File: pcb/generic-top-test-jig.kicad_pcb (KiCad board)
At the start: 2 copper layers, 45 x 39.2 mm, 13 parts, among them P1 CONN_01X16, U1 74HC4051, U2 74HC4067, U3 74HC4067, U4 74HC4067, U5 74HC4067

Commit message: Gerbers for v1 of the test jig.
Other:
- net class Default: clearance 0.1524 -> 0.14986
- net class Power: clearance 0.1524 -> 0.14986
- rule trace_clearance: 0.1524 -> 0.14986

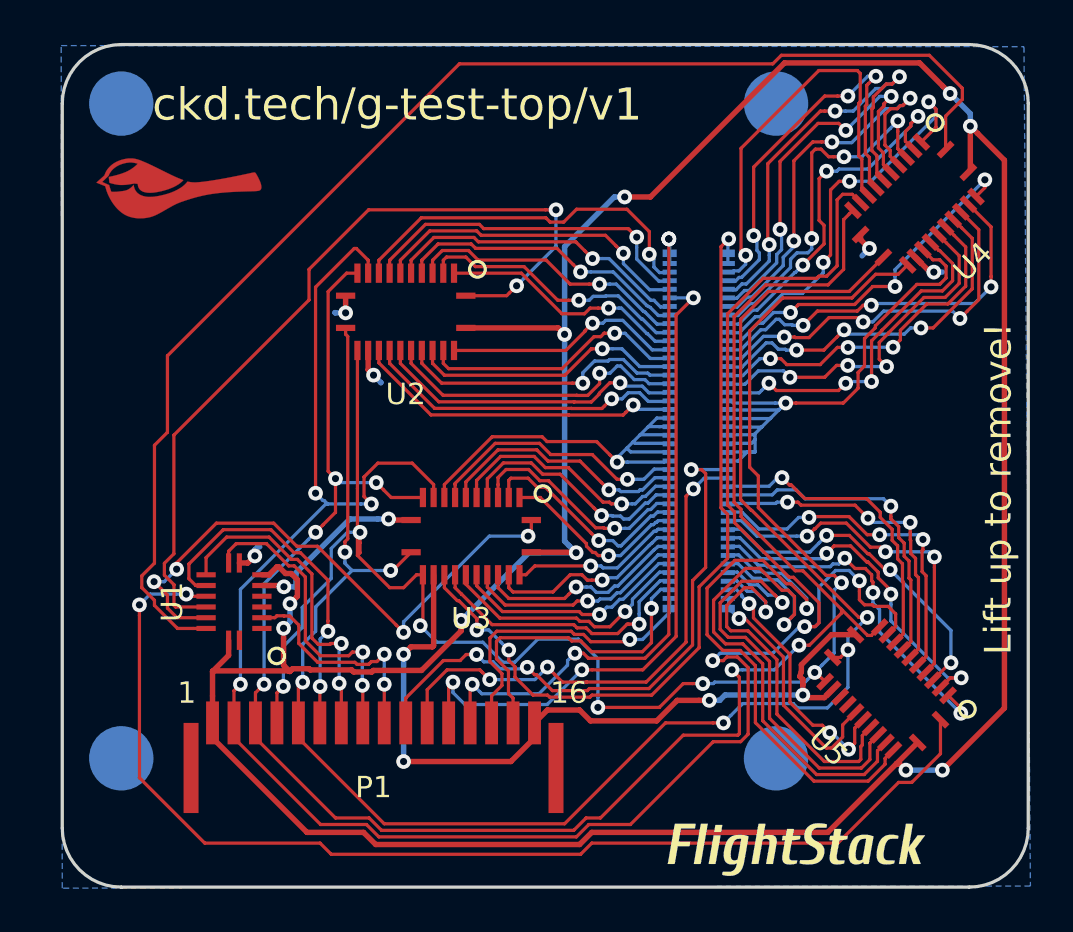
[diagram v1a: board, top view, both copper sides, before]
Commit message: Generic Test Jig Top v2 which correct Vee input in 8-way mux and changes SWD pins.
Also:
* Switches to thinner FlightStack logo.
* Adds OSHW logo.
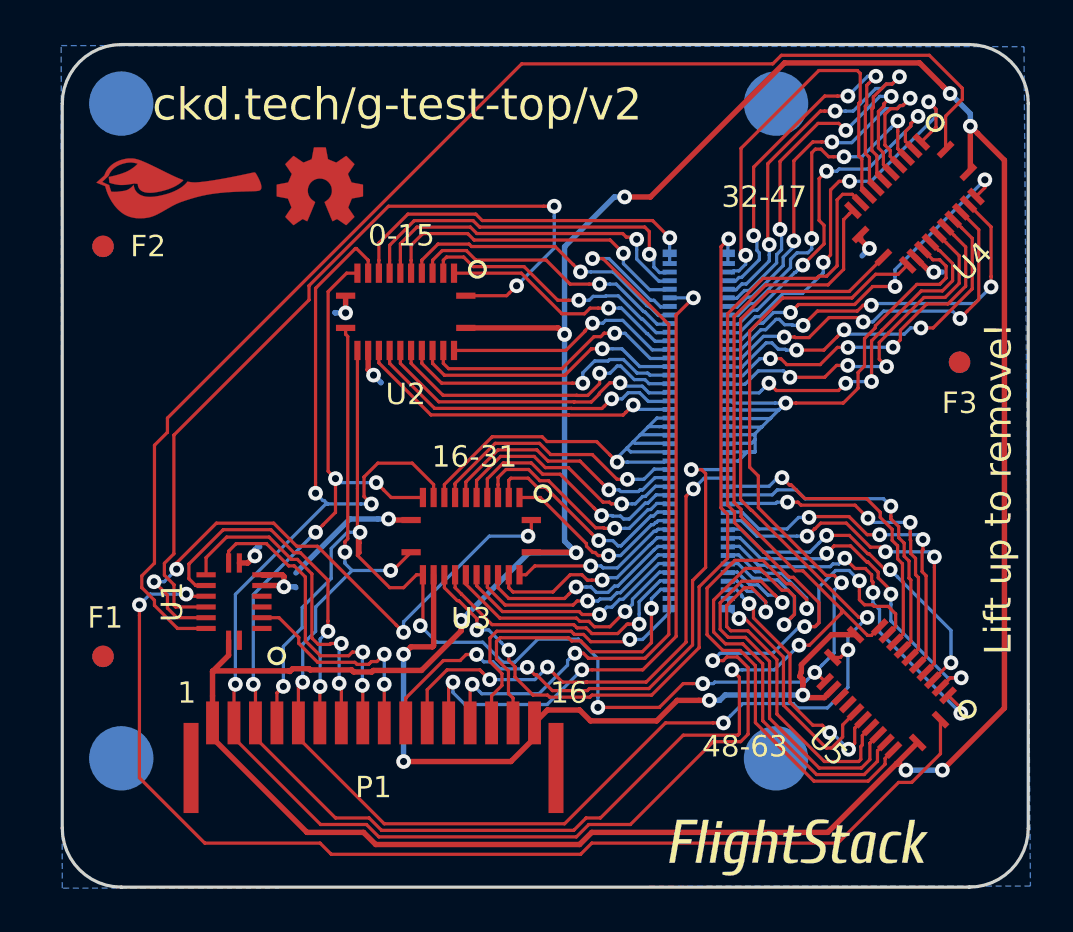
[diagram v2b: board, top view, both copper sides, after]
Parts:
- removed the G*** at (164.2, 127.5)
- added F1: 1mm, macrofab:Fiducial, F.Cu at (131.9, 118.5)
- added F2: 1mm, macrofab:Fiducial, F.Cu at (131.9, 99.4)
- added F3: 1mm, macrofab:Fiducial, F.Cu at (171.8, 104.8)
- added F4: 1mm, macrofab:Fiducial, B.Cu at (131.9, 118.5)
- added F5: 1mm, macrofab:Fiducial, B.Cu at (131.9, 99.4)
- added F6: 1mm, macrofab:Fiducial, B.Cu at (171.8, 104.8)
- added G***: LOGO, flightstack:flightstack_thin-12mm, F.Cu at (164.3, 127.4)
- added G***: OSHW, oshw:oshw-4mm, F.Cu at (142.0, 96.6)
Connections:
- PORT_IN1 pad 1: /SWCLK -> /TIM1
- PORT_IN1 pad 6: /GPIO2 -> /SWCLK
- U1 pad 7: +5V -> GNDPWR
- U2 pad 6: /GPIO2 -> /TIM4
- U2 pad 7: /TIM4 -> /TIM3
- U2 pad 8: /TIM3 -> /TIM2
- U2 pad 9: /TIM2 -> /TIM1
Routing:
- net /TIM1: track 0.00 -> 17.2 mm, vias 0 -> 1
- net /GPIO2: track 14.2 -> 0.00 mm, vias 1 -> 0
- net +5V: track 149.7 -> 143.0 mm, vias 10 -> 8
- net /SWCLK: track 32.2 -> 36.3 mm, vias 4 -> 3
- net /Z2: track 61.9 -> 60.2 mm
- net GNDPWR: track 52.8 -> 54.0 mm
- net /TIM2: track 17.2 -> 16.5 mm
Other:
- board text added: "0-15"
- board text added: "16-31"
- board text added: "32-47"
- board text added: "48-63"
- board text added: "ckd.tech/g-test-top/v2"
- board text removed: "ckd.tech/g-test-top/v1"

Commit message: Add decoupling caps.
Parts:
- added C1: 0.1uF, Capacitors_SMD:C_0603_HandSoldering, B.Cu at (149.1, 112.9)
- added C2: 0.1uF, Capacitors_SMD:C_0603_HandSoldering, B.Cu at (138.0, 116.0)
- added C3: 0.1uF, Capacitors_SMD:C_0603_HandSoldering, B.Cu at (145.9, 102.5)
- added C4: 0.1uF, Capacitors_SMD:C_0603_HandSoldering, B.Cu at (169.7, 97.4)
- added C5: 0.1uF, Capacitors_SMD:C_0603_HandSoldering, B.Cu at (168.4, 120.0)
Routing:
- net +5V: track 143.0 -> 156.6 mm, vias 8 -> 11
- net GNDPWR: track 54.0 -> 59.8 mm
- net /Z1: track 27.3 -> 28.8 mm
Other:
- board text added: "ckd.tech/g-test-top/v3"
- board text removed: "ckd.tech/g-test-top/v2"

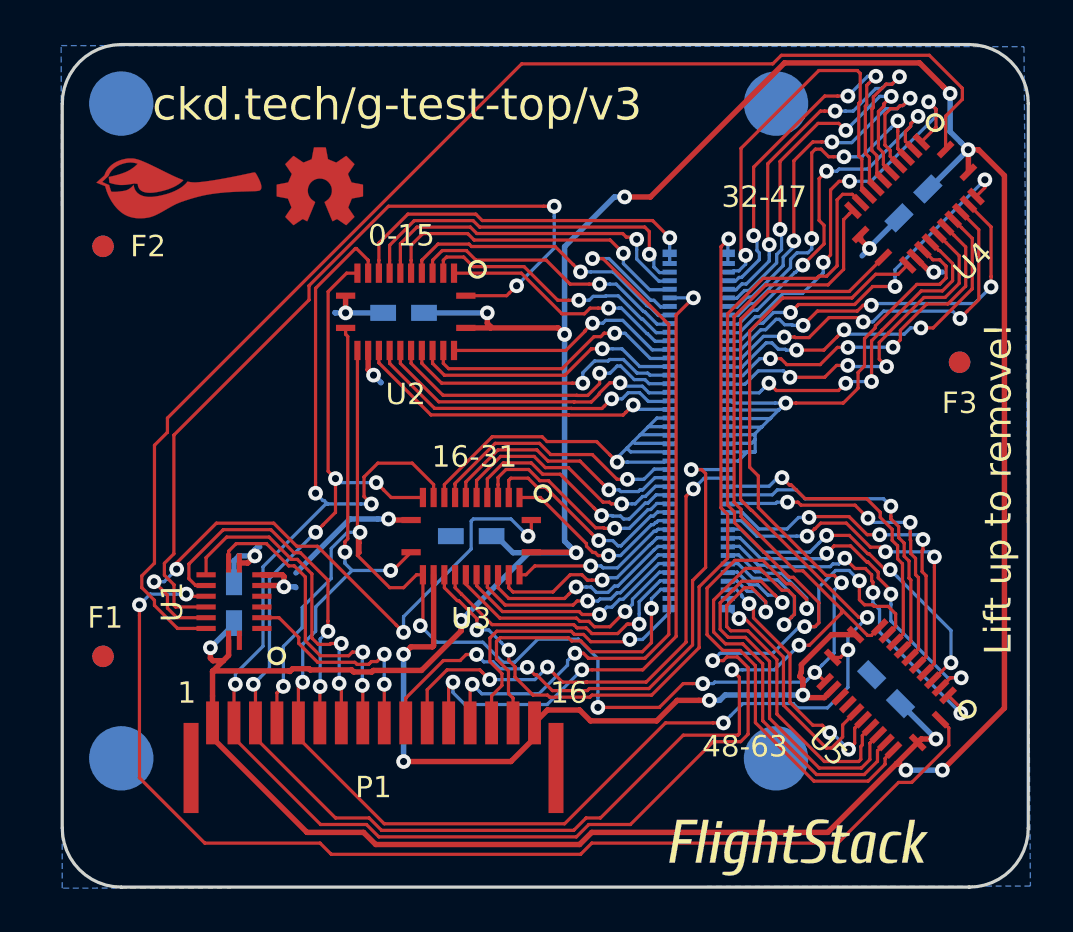
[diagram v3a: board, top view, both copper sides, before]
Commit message: Rebrand everything to Polystack and increment versions.
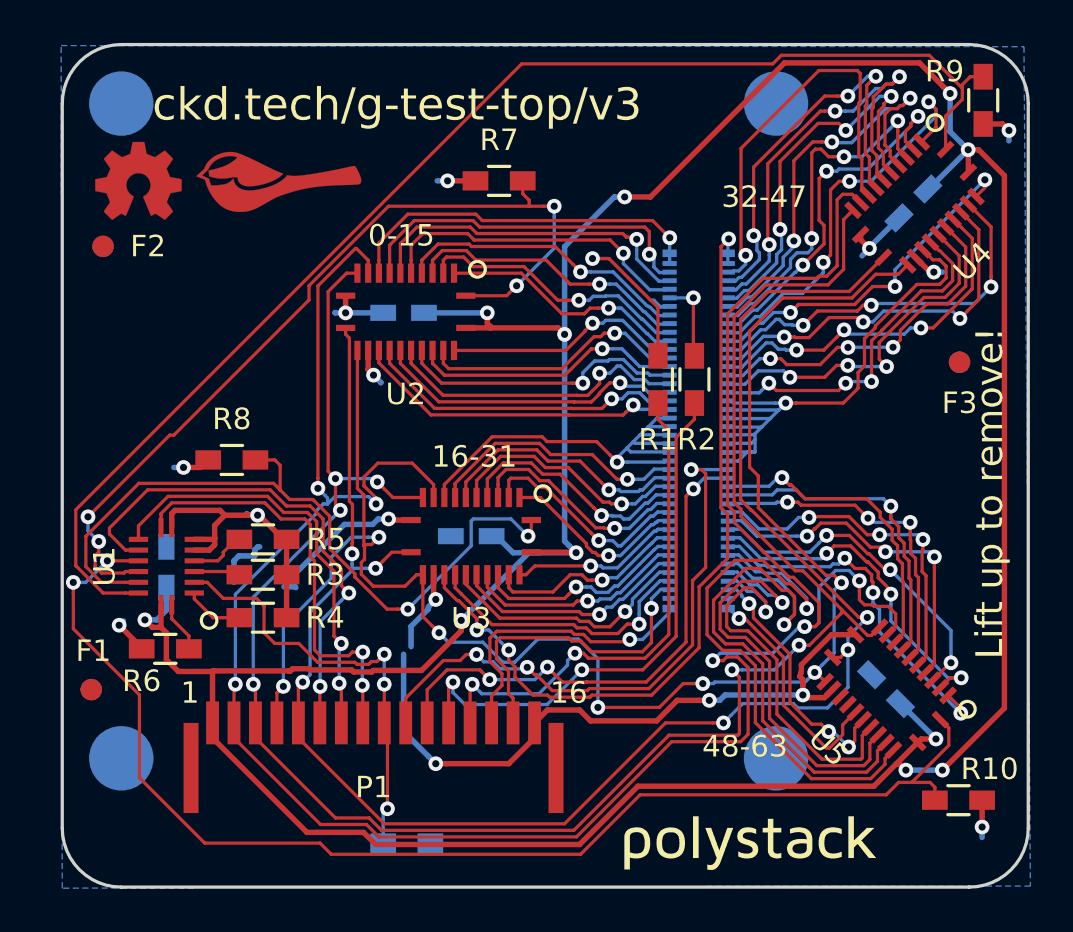
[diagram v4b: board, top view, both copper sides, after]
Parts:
- removed the G*** at (164.3, 127.4)
- added R1: 220, Resistors_SMD:R_0603_HandSoldering, F.Cu at (157.8, 105.6)
- added R10: 10k, Resistors_SMD:R_0603_HandSoldering, F.Cu at (171.8, 125.2)
- added R11: 10k, Resistors_SMD:R_0603_HandSoldering, B.Cu at (146.1, 127.2)
- added R2: 220, Resistors_SMD:R_0603_HandSoldering, F.Cu at (159.4, 105.6)
- added R3: 10k, Resistors_SMD:R_0603_HandSoldering, F.Cu at (139.3, 114.7)
- added R4: 10k, Resistors_SMD:R_0603_HandSoldering, F.Cu at (139.3, 116.7)
- added R5: 10k, Resistors_SMD:R_0603_HandSoldering, F.Cu at (139.3, 113.0)
- added R6: 10k, Resistors_SMD:R_0603_HandSoldering, F.Cu at (134.8, 118.2)
- added R7: 10k, Resistors_SMD:R_0603_HandSoldering, F.Cu at (150.3, 96.3)
- added R8: 10k, Resistors_SMD:R_0603_HandSoldering, F.Cu at (137.9, 109.3)
- added R9: 10k, Resistors_SMD:R_0603_HandSoldering, F.Cu at (172.9, 92.6)
- added svg2mod: G***, polystack:polystack-medium-0.625, B.Cu at (162.1, 127.2)
- added svg2mod: G***, polystack:polystack-medium-0.625, F.Cu at (162.1, 127.2)
- moved G*** 8.45 mm to (133.6, 96.3)
- moved G*** 4.66 mm to (140.1, 96.4)
- moved C2 3.56 mm to (134.8, 114.3)
- moved U1 3.56 mm to (134.8, 114.3)
- moved F1 1.64 mm to (131.3, 120.0)
- moved F4 1.64 mm to (131.3, 120.0)
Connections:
- P1 pad 12: /SWDIO -> Net-(P1-Pad12)
- P1 pad 13: /SWCLK -> Net-(P1-Pad13)
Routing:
- net /SWDIO: track 31.6 -> 3.83 mm, vias 3 -> 1
- net /SWCLK: track 36.3 -> 10.6 mm, vias 3 -> 1
- net Net-(P1-Pad12): track 0.00 -> 25.6 mm, vias 0 -> 2
- net Net-(P1-Pad13): track 0.00 -> 23.6 mm, vias 0 -> 2
- net GNDPWR: track 59.8 -> 74.4 mm, vias 11 -> 15
- net /Z: track 10.2 -> 20.3 mm, vias 2 -> 3
- net /S4: track 16.5 -> 23.8 mm
- net /Z1: track 28.8 -> 35.1 mm, vias 4 -> 2
- net /S6: track 14.2 -> 19.9 mm
- net /S5: track 15.1 -> 19.9 mm
- net /Z3: track 54.0 -> 58.2 mm
- net +5V: track 156.6 -> 160.2 mm
- net (no net): track 0.00 -> 3.21 mm
- net Net-(R4-Pad2): track 0.00 -> 2.74 mm
- net Net-(R5-Pad2): track 0.00 -> 2.60 mm
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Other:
- rule pad_to_mask_clearance: 0.2 -> 0.0762

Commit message: Final gerbers for test manufacturing run.
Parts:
- moved P1 0.90 mm to (144.5, 123.2)
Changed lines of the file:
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@@
 (kicad_pcb (version 4) (host pcbnew 4.0.1-stable)
   (general
-    (links 0)
+    (links 154)
     (no_connects 0)
-    (area 129.924999 89.924999 175.075001 129.325001)
+    (area 118.127143 74.1 268.690476 178)
     (thickness 1.6)
     (drawings 33)
@@
     (visible_elements FFFFFF7F)
     (pcbplotparams
-      (layerselection 0x010f0_80000001)
+      (layerselection 0x010fc_80000001)
       (usegerberextensions true)
       (excludeedgelayer true)
@@
     (add_net +5V)
     (add_net GNDPWR)
+  )
+  (module fci:SFW12LF-16pin (layer F.Cu)
+    (at 144.5 123.2)
+    (fp_text reference P1 (at 0 1.4) (layer F.SilkS)
+      (effects (font (size 1 1) (thickness 0.15)))
+    )
+    (fp_text value CONN_01X16 (at 0 0.4) (layer F.Fab)
+      (effects (font (size 1 1) (thickness 0.15)))
+    )
+    (fp_line (start -11 6) (end 11 6) (layer F.CrtYd) (width 0.15))
+    (pad 1 smd rect (at -7.5 -1.6) (size 0.6 2) (layers F.Cu F.Paste F.Mask)
+      (net 2 +5V))
+    (pad 2 smd rect (at -6.5 -1.6) (size 0.6 2) (layers F.Cu F.Paste F.Mask)
+      (net 3 /S0))
+    (pad 3 smd rect (at -5.5 -1.6) (size 0.6 2) (layers F.Cu F.Paste F.Mask)
+      (net 4 /S1))
+    (pad 4 smd rect (at -4.5 -1.6) (size 0.6 2) (layers F.Cu F.Paste F.Mask)
+      (net 5 /S2))
+    (pad 5 smd rect (at -3.5 -1.6) (size 0.6 2) (layers F.Cu F.Paste F.Mask)
+      (net 6 /S3))
+    (pad 6 smd rect (at -2.5 -1.6) (size 0.6 2) (layers F.Cu F.Paste F.Mask)
+      (net 7 /S4))
+    (pad 7 smd rect (at -1.5 -1.6) (size 0.6 2) (layers F.Cu F.Paste F.Mask)
+      (net 8 /S5))
+    (pad 8 smd rect (at -0.5 -1.6) (size 0.6 2) (layers F.Cu F.Paste F.Mask)
+      (net 9 /S6))
+    (pad 9 smd rect (at 0.5 -1.6) (size 0.6 2) (layers F.Cu F.Paste F.Mask)
+      (net 10 /Z))
+    (pad 10 smd rect (at 1.5 -1.6) (size 0.6 2) (layers F.Cu F.Paste F.Mask)
+      (net 11 /BOOT))
+    (pad 11 smd rect (at 2.5 -1.6) (size 0.6 2) (layers F.Cu F.Paste F.Mask)
+      (net 12 /RESET))
+    (pad 12 smd rect (at 3.5 -1.6) (size 0.6 2) (layers F.Cu F.Paste F.Mask)
+      (net 85 "Net-(P1-Pad12)"))
+    (pad 13 smd rect (at 4.5 -1.6) (size 0.6 2) (layers F.Cu F.Paste F.Mask)
+      (net 86 "Net-(P1-Pad13)"))
+    (pad 14 smd rect (at 5.5 -1.6) (size 0.6 2) (layers F.Cu F.Paste F.Mask)
+      (net 15 /RX))
+    (pad 15 smd rect (at 6.5 -1.6) (size 0.6 2) (layers F.Cu F.Paste F.Mask)
+      (net 16 /TX))
+    (pad 16 smd rect (at 7.5 -1.6) (size 0.6 2) (layers F.Cu F.Paste F.Mask)
+      (net 1 GNDPWR))
+    (pad "" smd rect (at -8.5 0.5) (size 0.7 4.2) (layers F.Cu F.Paste F.Mask))
+    (pad "" smd rect (at 8.5 0.5) (size 0.7 4.2) (layers F.Cu F.Paste F.Mask))
   )
   (module polystack:polystack-medium-0.625 (layer B.Cu)
@@
       (net 16 /TX))
   )
-  (module fci:SFW12LF-16pin (layer F.Cu)
-    (at 144.5 124.1)
-    (fp_text reference P1 (at 0 0.5) (layer F.SilkS)
-      (effects (font (size 1 1) (thickness 0.15)))
-    )
-    (fp_text value CONN_01X16 (at 0 -0.5) (layer F.Fab)
-      (effects (font (size 1 1) (thickness 0.15)))
-    )
-    (fp_line (start -11 5.1) (end 11 5.1) (layer F.CrtYd) (width 0.15))
-    (pad 1 smd rect (at -7.5 -2.5) (size 0.6 2) (layers F.Cu F.Paste F.Mask)
-      (net 2 +5V))
-    (pad 2 smd rect (at -6.5 -2.5) (size 0.6 2) (layers F.Cu F.Paste F.Mask)
-      (net 3 /S0))
-    (pad 3 smd rect (at -5.5 -2.5) (size 0.6 2) (layers F.Cu F.Paste F.Mask)
-      (net 4 /S1))
-    (pad 4 smd rect (at -4.5 -2.5) (size 0.6 2) (layers F.Cu F.Paste F.Mask)
-      (net 5 /S2))
-    (pad 5 smd rect (at -3.5 -2.5) (size 0.6 2) (layers F.Cu F.Paste F.Mask)
-      (net 6 /S3))
-    (pad 6 smd rect (at -2.5 -2.5) (size 0.6 2) (layers F.Cu F.Paste F.Mask)
-      (net 7 /S4))
-    (pad 7 smd rect (at -1.5 -2.5) (size 0.6 2) (layers F.Cu F.Paste F.Mask)
-      (net 8 /S5))
-    (pad 8 smd rect (at -0.5 -2.5) (size 0.6 2) (layers F.Cu F.Paste F.Mask)
-      (net 9 /S6))
-    (pad 9 smd rect (at 0.5 -2.5) (size 0.6 2) (layers F.Cu F.Paste F.Mask)
-      (net 10 /Z))
-    (pad 10 smd rect (at 1.5 -2.5) (size 0.6 2) (layers F.Cu F.Paste F.Mask)
-      (net 11 /BOOT))
-    (pad 11 smd rect (at 2.5 -2.5) (size 0.6 2) (layers F.Cu F.Paste F.Mask)
-      (net 12 /RESET))
-    (pad 12 smd rect (at 3.5 -2.5) (size 0.6 2) (layers F.Cu F.Paste F.Mask)
-      (net 85 "Net-(P1-Pad12)"))
-    (pad 13 smd rect (at 4.5 -2.5) (size 0.6 2) (layers F.Cu F.Paste F.Mask)
-      (net 86 "Net-(P1-Pad13)"))
-    (pad 14 smd rect (at 5.5 -2.5) (size 0.6 2) (layers F.Cu F.Paste F.Mask)
-      (net 15 /RX))
-    (pad 15 smd rect (at 6.5 -2.5) (size 0.6 2) (layers F.Cu F.Paste F.Mask)
-      (net 16 /TX))
-    (pad 16 smd rect (at 7.5 -2.5) (size 0.6 2) (layers F.Cu F.Paste F.Mask)
-      (net 1 GNDPWR))
-    (pad "" smd rect (at -8.5 -0.4) (size 0.7 4.2) (layers F.Cu F.Paste F.Mask))
-    (pad "" smd rect (at 8.5 -0.4) (size 0.7 4.2) (layers F.Cu F.Paste F.Mask))
-  )
   (module "nxp:SOT763-1(DHVQFN16)" (layer F.Cu)

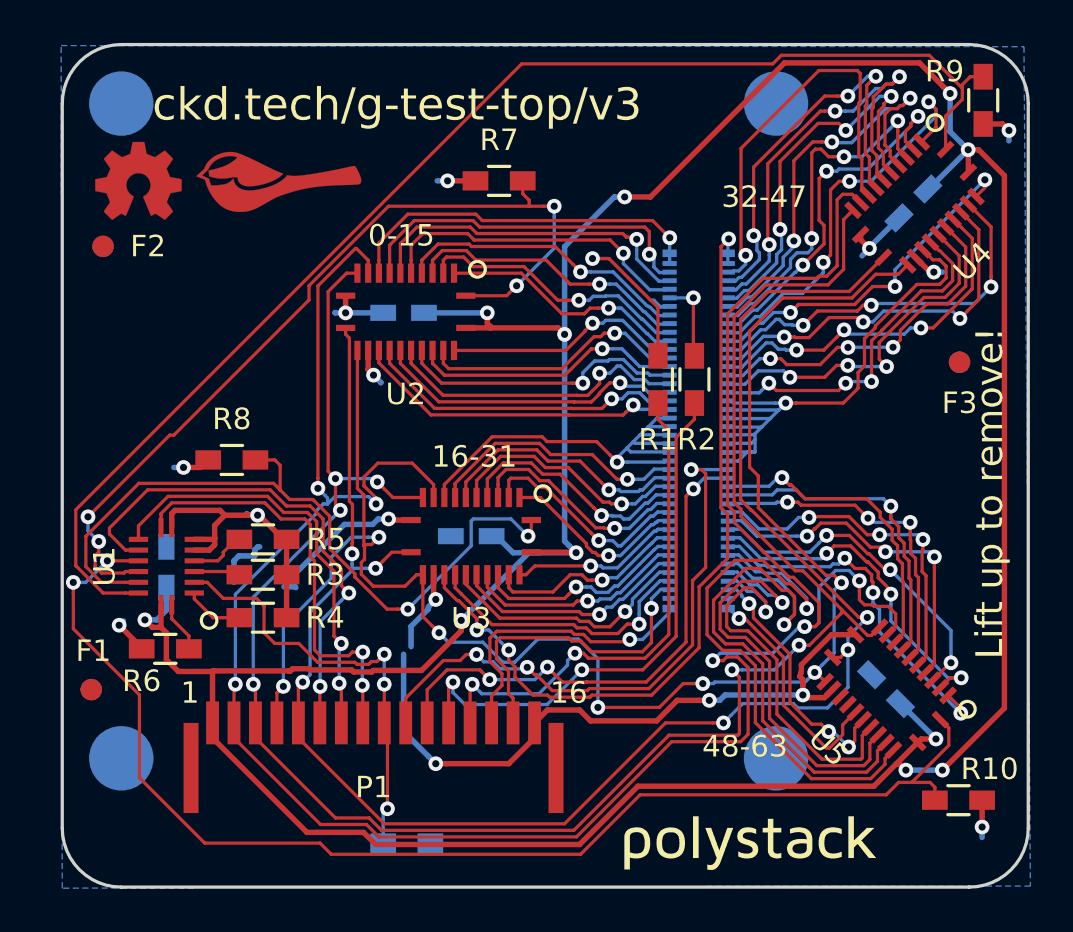
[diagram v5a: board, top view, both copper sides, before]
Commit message: Update polystack logo to bold variant and bump version number.
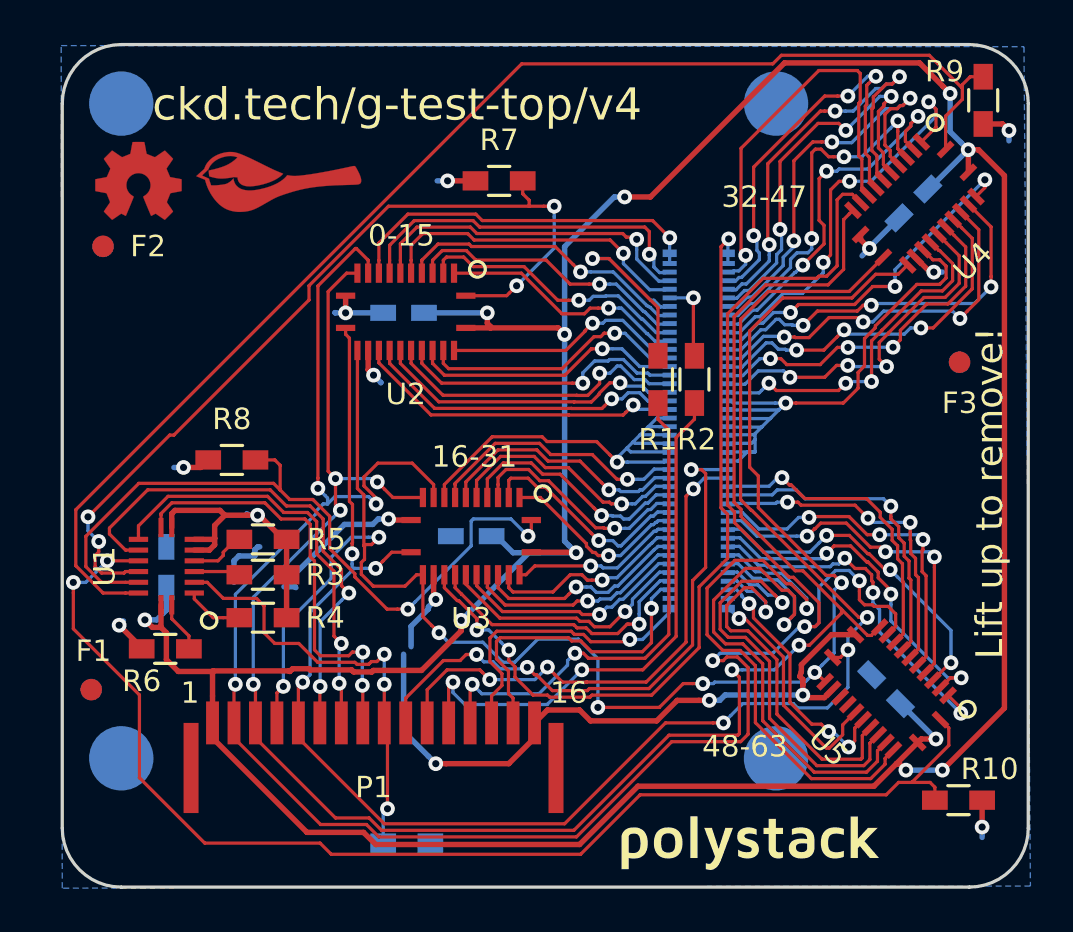
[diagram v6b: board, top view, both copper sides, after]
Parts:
- svg2mod (x2): footprint polystack:polystack-medium-0.625 -> polystack:polystack-bold-0.625
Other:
- board text added: "ckd.tech/g-test-top/v4"
- board text removed: "ckd.tech/g-test-top/v3"
